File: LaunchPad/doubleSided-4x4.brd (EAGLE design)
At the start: 100 x 100 mm, 32 parts

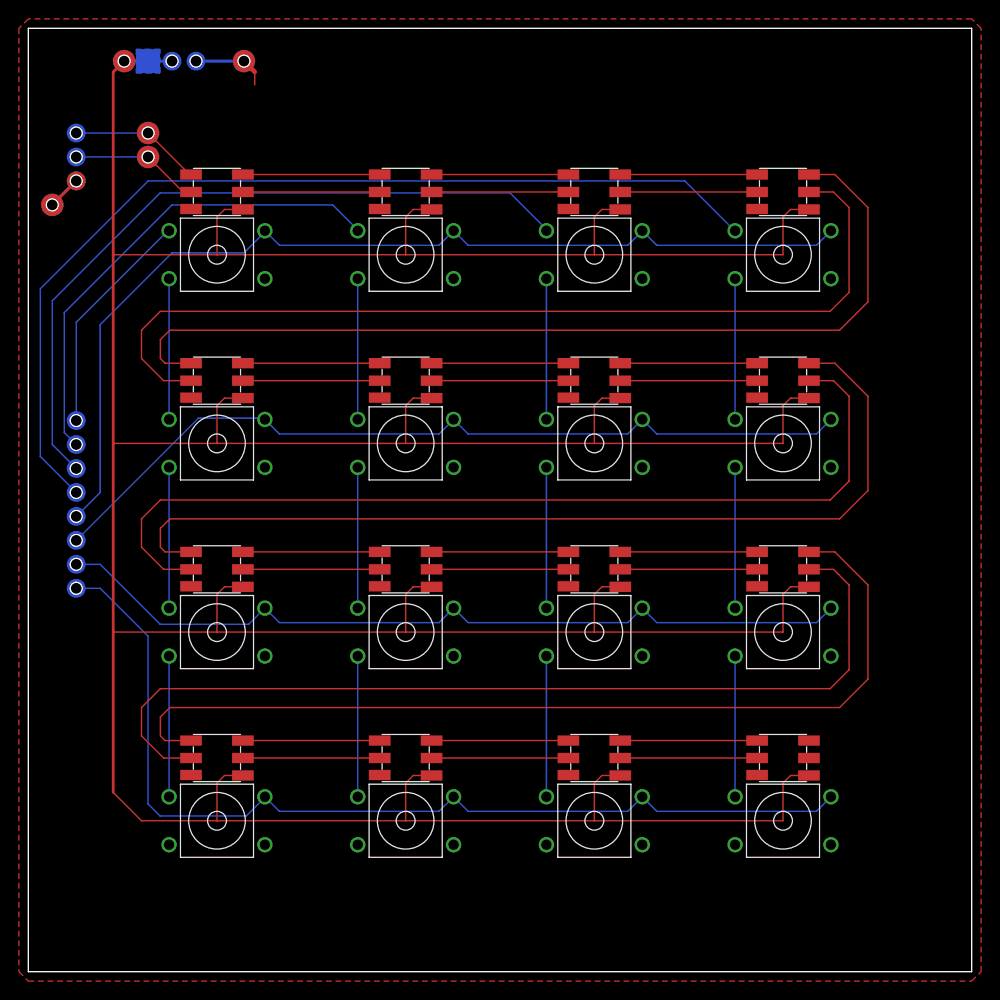
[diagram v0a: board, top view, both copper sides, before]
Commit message: Made clearanes for othermill
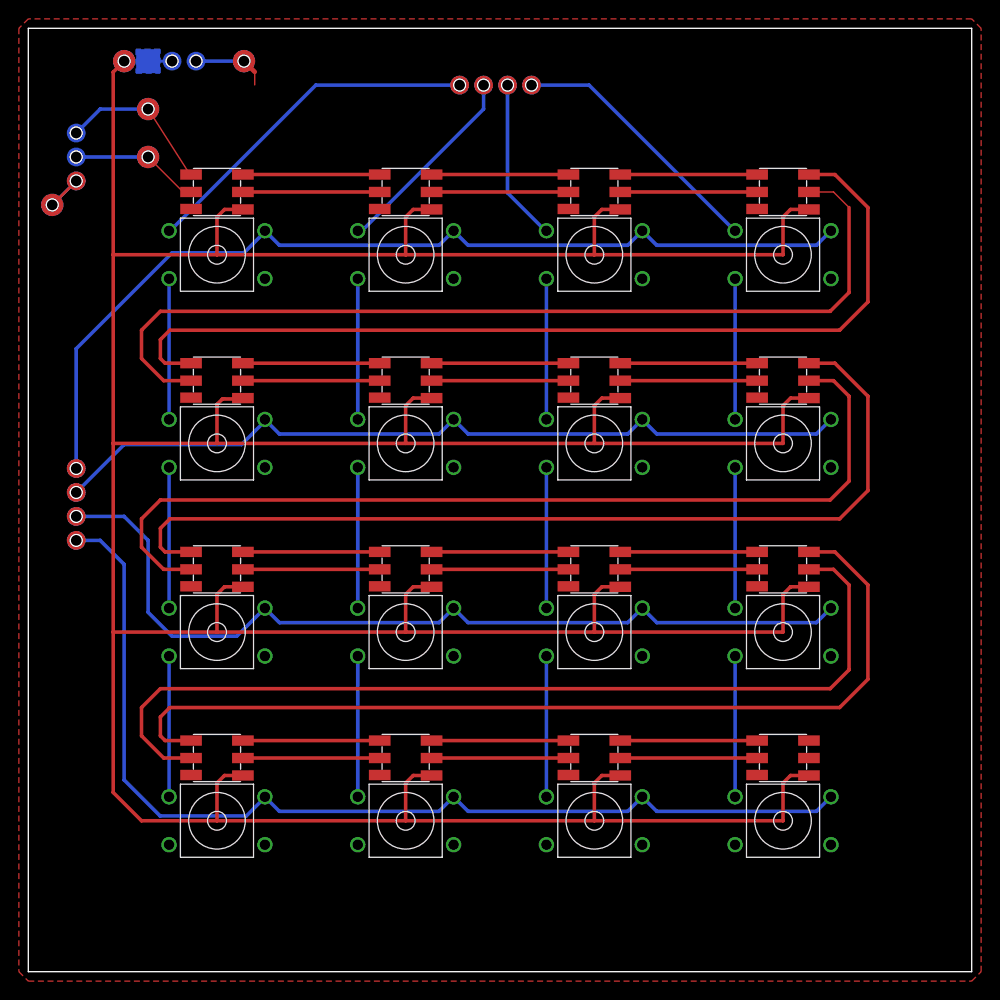
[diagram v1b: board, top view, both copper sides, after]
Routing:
- net N$34: track 103.8 -> 17.2 mm
- net N$38: track 41.3 -> 0.00 mm
- net N$32: track 77.5 -> 36.8 mm
- net N$39: track 0.00 -> 31.1 mm
- net N$37: track 23.4 -> 46.4 mm
- net N$35: track 43.0 -> 23.2 mm
- net N$31: track 51.6 -> 37.9 mm
- net DATA5: track 14.0 -> 17.0 mm
- net 5V: track 481.6 -> 484.6 mm
- net N$33: track 24.1 -> 21.1 mm
- net N$36: track 25.4 -> 28.0 mm
